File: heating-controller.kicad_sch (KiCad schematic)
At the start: 0 parts

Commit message: Name the board Andiron v1.0; add BOM with cost estimates, renders, getting-started docs and CLAUDE.md
- Andiron v1.0 and the author name on the silkscreen, in every title block
  and in the README; J116 warning moved inside the board edge.
- tools/bom.py: BOM from the schematic with LCSC prices from the Konnect
  JLCPCB database -> docs/BOM.md (cost summary, Basic/Extended, DNP list) and
  docs/bom/andiron-bom-jlc.csv (JLCPCB upload). ~$15.77 components per board,
  ~$28.97 per board at 5 including assumed Extended-part fees.
- tools/sync_models.py relinks all 152 footprints to 3D models with portable
  ${KIPRJMOD} paths (also fixed in lib/jlc.pretty); stand-ins for the
  ESP32-C6 module and HRO USB-C. Wired into the routing pipeline.
- tools/render.sh: ray-traced 3D views and 2D layer plots in docs/images/.
- README rewritten: renders, BOM summary, getting started with Konnect MCP,
  repository layout. tools/README.md indexes every script; Konnect helpers
  and the pour-island check moved into tools/.
- CLAUDE.md: BOM and cost estimate kept current on every schematic change,
  definition of done for board changes.
- .konnect/project.json design rules brought in line with what is built;
  project-local .mcp.json for Konnect.
- Removed references to a commercial product; the docs now describe the
  board on its own terms, designed for Home Assistant and ESPHome.

ERC 0 errors; DRC 0 errors, 0 unconnected, parity clean.

Co-Authored-By: Claude Opus 5.5 <noreply@anthropic.com>
Claude-Session: https://claude.ai/code/session_01XDSh2Z4phxf7z2Gu1153CL
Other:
- company: (none) -> Cedric Van Goethem
- title: (none) -> Andiron
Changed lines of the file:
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@@
 	(generator_version "10.0")
 	(paper "A4")
+	(title_block
+		(title "Andiron")
+		(date "2026-10-22")
+		(rev "v1.0")
+		(company "Cedric Van Goethem")
+	)
   (sheet
 		(at 30 40)

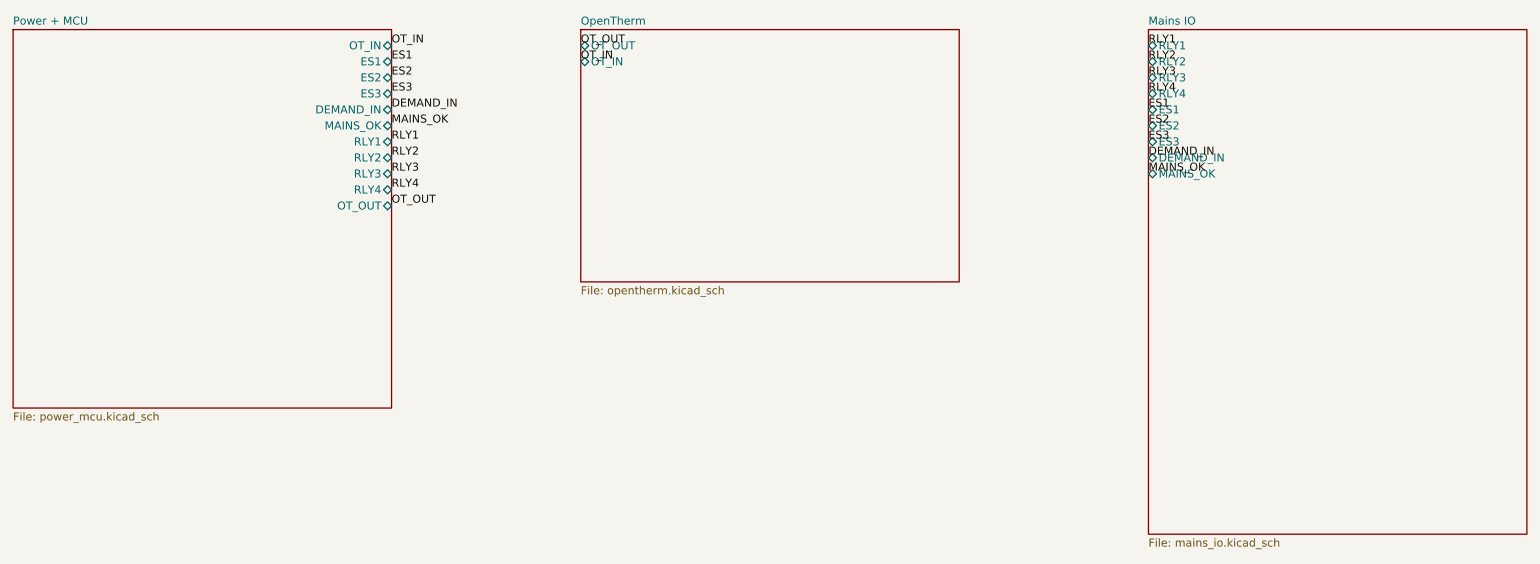
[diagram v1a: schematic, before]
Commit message: Andiron v1.0 redesign: volt-free changeover relays, no mains sensing, layout by module area
- Relays: four HF115F/005-1ZS3A changeover relays (CH1-CH4), each with its own
  NC/COM/NO terminal, as UK heating controllers present their outputs; 5 kV
  VDE-reinforced coil-to-contact insulation. Each channel is its own net class
  and keeps 6.4 mm clearance and creepage from everything that is not itself.
- Removed the 230 V supply input, L/N rails and all five mains sensing inputs
  (30 resistors, 5 optos, end-switch and demand terminals). The only mains on
  the board is the relay contacts.
- Power: LDL1117S33R replaces the AMS1117 (0.35 V dropout, ceramic-stable,
  18 V abs-max, no heat-spreading copper); relays run from USB 5 V directly.
- OLED header fixed to GND/3V3/SCL/SDA (option resistors removed); freed GPIOs
  on an 8-pin spare header; Mains IO sheet renamed Relays.
- Layout regenerated by module area (relay strip, drivers, MCU with antenna at
  the left edge, power, OpenTherm, sensors, controls), 150 x 90 mm. Placement
  and shared geometry now in tools/layout/; tools/sync_netlist.py syncs the
  schematic to the board headlessly.
- Low-voltage clearance 0.25 mm so module pins escape straight out; USB nets
  get their own 0.2 mm class. Pipeline widens router neck-down stubs; stitching
  and island-repair vias avoid pads.
- Silkscreen relabelled in plain language (CH1 NC COM NO, OPENTHERM, FLOW TEMP,
  OUTDOOR TEMP, ...); repository URL removed.
- Docs: requirements and design brief rewritten for v1.0, schematic plan,
  README, BOM, renders, schematic PDF and layout lessons updated.

ERC 0 errors; DRC 0 errors, 0 unconnected, parity clean; sanity PASS.
BOM: ~$15.77 -> ~$24.03 components per board (~$28.97 -> ~$37.23 at 5 incl.
fees), mostly the four HF115F relays.

Co-Authored-By: Claude Opus 5.5 <noreply@anthropic.com>
Claude-Session: https://claude.ai/code/session_01XDSh2Z4phxf7z2Gu1153CL
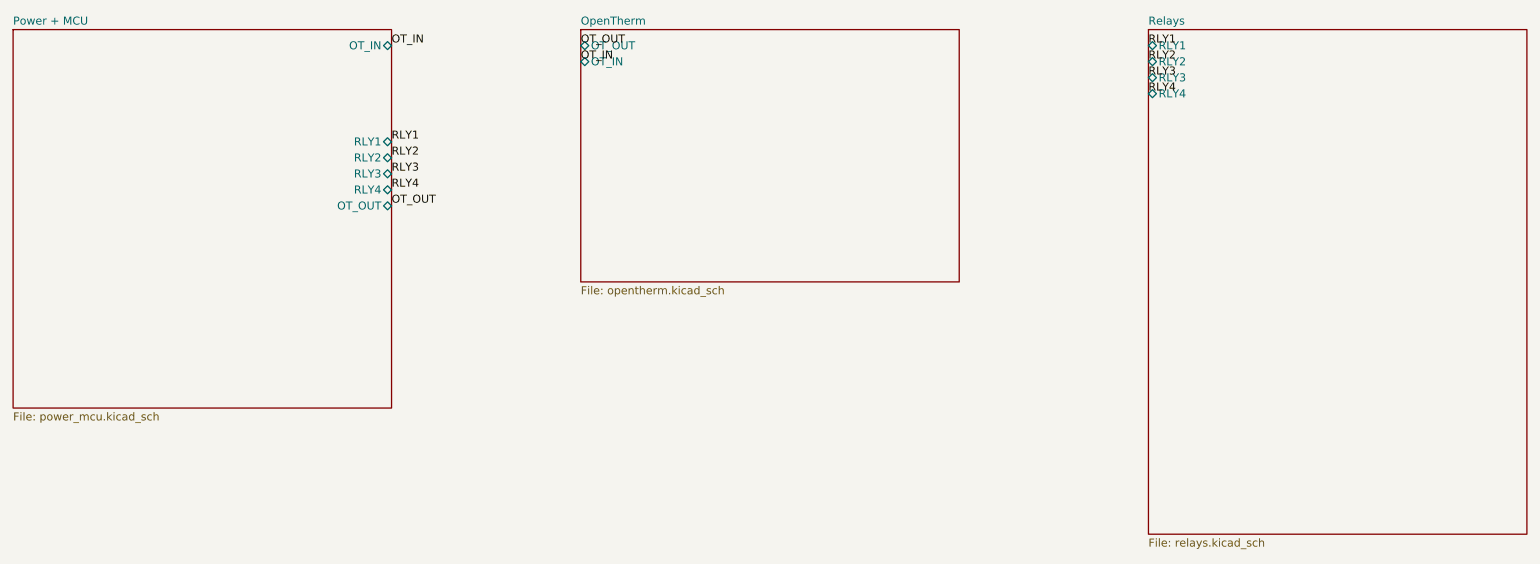
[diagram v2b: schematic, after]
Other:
- sheet Mains IO renamed Relays
- sheet Power + MCU ports: added none; removed DEMAND_IN, ES1, ES2, ES3, MAINS_OK
- sheet Relays: file mains_io.kicad_sch -> relays.kicad_sch
- sheet Relays ports: added none; removed DEMAND_IN, ES1, ES2, ES3, MAINS_OK
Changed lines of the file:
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@@
 			(at 90 42.54 0)
-		)
-		(pin "ES1" bidirectional
-			(at 90 45.08 0)
-		)
-		(pin "ES2" bidirectional
-			(at 90 47.62 0)
-		)
-		(pin "ES3" bidirectional
-			(at 90 50.16 0)
-		)
-		(pin "DEMAND_IN" bidirectional
-			(at 90 52.7 0)
-		)
-		(pin "MAINS_OK" bidirectional
-			(at 90 55.24 0)
 		)
 		(pin "RLY1" bidirectional
@@
 			(color 0 0 0 0.0)
 		)
-		(property "Sheetname" "Mains IO"
+		(property "Sheetname" "Relays"
 			(at 210 39.365 0)
 			(show_name no)
@@
 			)
 		)
-		(property "Sheetfile" "mains_io.kicad_sch"
+		(property "Sheetfile" "relays.kicad_sch"
 			(at 210 120.635 0)
 			(show_name no)
@@
 		(pin "RLY4" bidirectional
 			(at 210 50.16 180)
-		)
-		(pin "ES1" bidirectional
-			(at 210 52.7 180)
-		)
-		(pin "ES2" bidirectional
-			(at 210 55.24 180)
-		)
-		(pin "ES3" bidirectional
-			(at 210 57.78 180)
-		)
-		(pin "DEMAND_IN" bidirectional
-			(at 210 60.32 180)
-		)
-		(pin "MAINS_OK" bidirectional
-			(at 210 62.86 180)
 		)
 		(instances
@@
 		)
 	)
-	(label "ES1"
-		(at 90.00 45.08 0)
-		(effects
-			(font
-				(size 1.27 1.27)
-			)
-			(justify left bottom)
-		)
-	)
-	(label "ES2"
-		(at 90.00 47.62 0)
-		(effects
-			(font
-				(size 1.27 1.27)
-			)
-			(justify left bottom)
-		)
-	)
-	(label "ES3"
-		(at 90.00 50.16 0)
-		(effects
-			(font
-				(size 1.27 1.27)
-			)
-			(justify left bottom)
-		)
-	)
-	(label "DEMAND_IN"
-		(at 90.00 52.70 0)
-		(effects
-			(font
-				(size 1.27 1.27)
-			)
-			(justify left bottom)
-		)
-	)
-	(label "MAINS_OK"
-		(at 90.00 55.24 0)
-		(effects
-			(font
-				(size 1.27 1.27)
-			)
-			(justify left bottom)
-		)
-	)
 	(label "RLY1"
 		(at 90.00 57.78 0)
@@
 		(effects
 			(font
-				(size 1.27 1.27)
-			)
-			(justify left bottom)
-		)
-	)
-	(label "ES1"
-		(at 210.00 52.70 0)
-		(effects
-			(font
-				(size 1.27 1.27)
-			)
-			(justify left bottom)
-		)
-	)
-	(label "ES2"
-		(at 210.00 55.24 0)
-		(effects
-			(font
-				(size 1.27 1.27)
-			)
-			(justify left bottom)
-		)
-	)
-	(label "ES3"
-		(at 210.00 57.78 0)
-		(effects
-			(font
-				(size 1.27 1.27)
-			)
-			(justify left bottom)
-		)
-	)
-	(label "DEMAND_IN"
-		(at 210.00 60.32 0)
-		(effects
-			(font
-				(size 1.27 1.27)
-			)
-			(justify left bottom)
-		)
-	)
-	(label "MAINS_OK"
-		(at 210.00 62.86 0)
-		(effects
-			(font
